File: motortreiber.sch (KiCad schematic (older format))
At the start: 40 parts, among them P15 STP_Y, P16 STP_E0, P17 STP_X, P18 STP_E1, P19 STP_Z, U3 A4988-BO, U4 A4988-BO, U5 A4988-BO, U6 A4988-BO, U7 A4988-BO

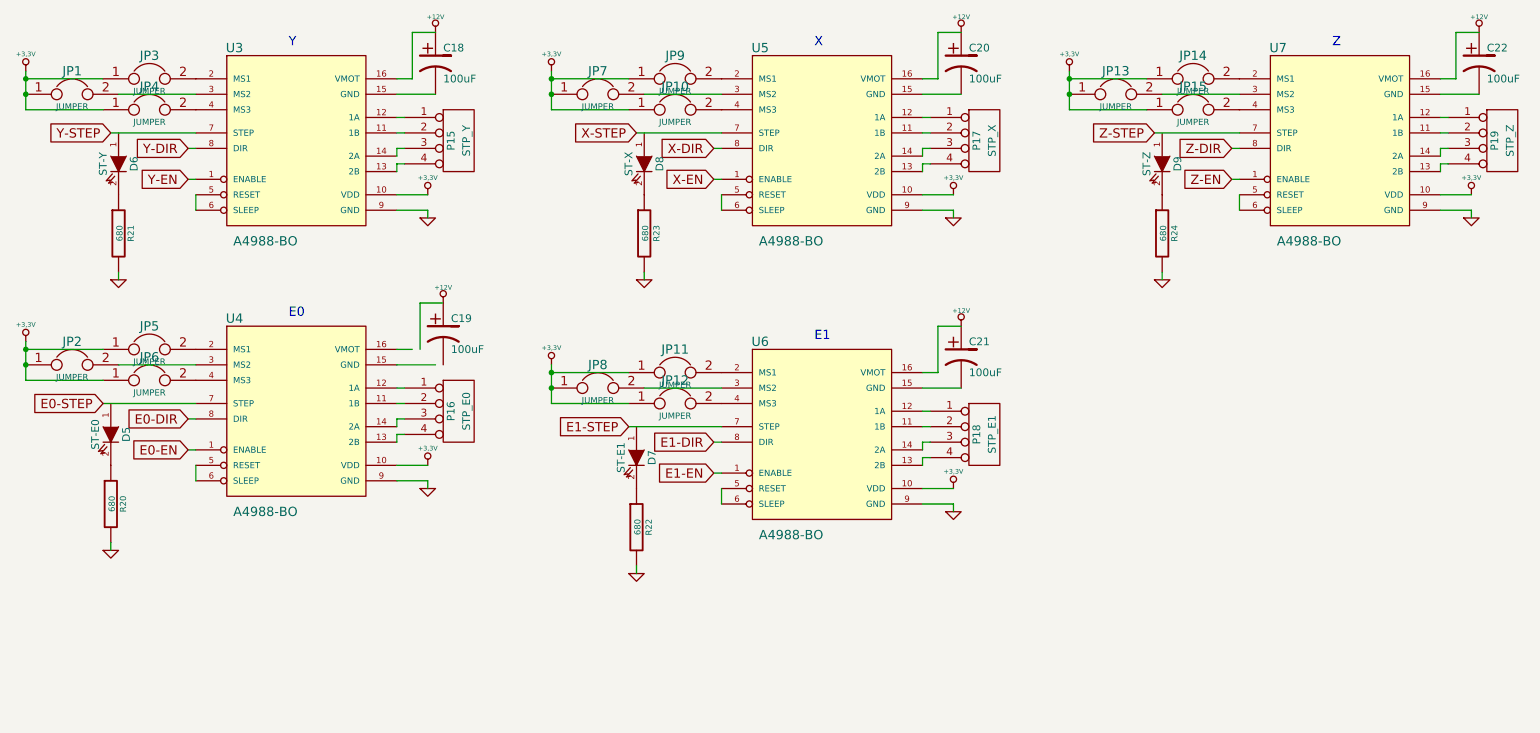
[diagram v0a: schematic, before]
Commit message: * Changed connectors to PSK type - this prevents plugging the steppers in the wrong way * Changed stepping increment jumpers to DIP-switches - easier setting
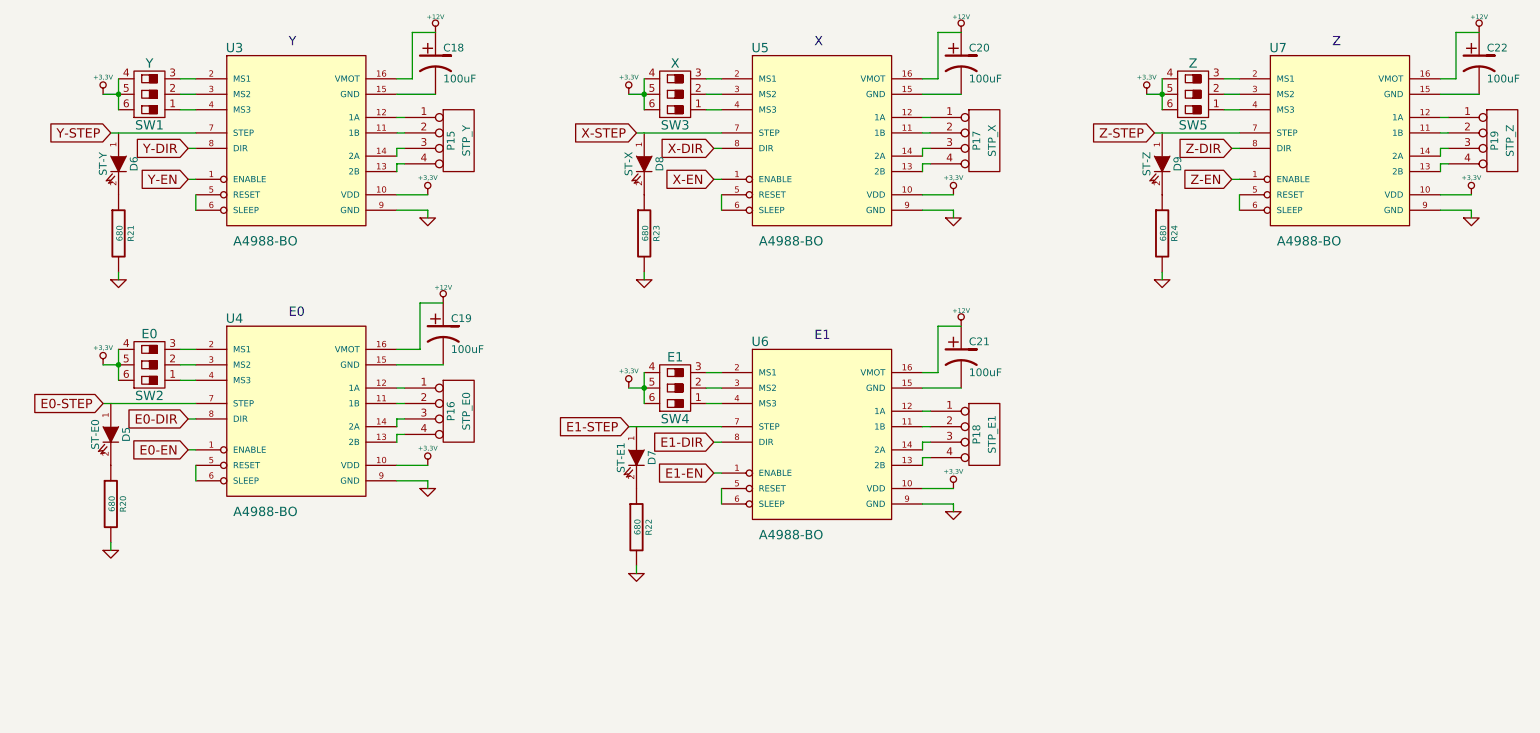
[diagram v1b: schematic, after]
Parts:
- removed JP1, JP10, JP11, JP12, JP13, JP14, JP15, JP2, JP3, JP4, JP5, JP6, JP7, JP8, JP9: JUMPER, ~, symbol JUMPER
- added SW1: Y, symbol DIPS_03
- added SW2: E0, symbol DIPS_03
- added SW3: X, symbol DIPS_03
- added SW4: E1, symbol DIPS_03
- added SW5: Z, symbol DIPS_03
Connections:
- net +12V: now also U4.16 (VMOT)
- net +3.3V: now also SW1.4, SW1.5, SW1.6, SW2.4, SW2.5, SW2.6, SW3.4, SW3.5, SW3.6, SW4.4, SW4.5, SW4.6, SW5.4, SW5.5, SW5.6
- net at U3.2 (MS1): now also SW1.3
- net at U3.3 (MS2): now also SW1.2
- net at U3.4 (MS3): now also SW1.1
- net at U5.2 (MS1): now also SW3.3
- net at U5.3 (MS2): now also SW3.2
- net at U5.4 (MS3): now also SW3.1
- net at U7.2 (MS1): now also SW5.3
- net at U7.3 (MS2): now also SW5.2
- net at U7.4 (MS3): now also SW5.1
- net at U4.15 (GND): now also C19.2
- net at U4.2 (MS1): now also SW2.3
- net at U4.3 (MS2): now also SW2.2
- net at U4.4 (MS3): now also SW2.1
- net at U6.2 (MS1): now also SW4.3
- net at U6.3 (MS2): now also SW4.2
- net at U6.4 (MS3): now also SW4.1

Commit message: * Removed numerous errors, schematic now passes ERC test. * Arranged footprints on PCB to prepare for routing
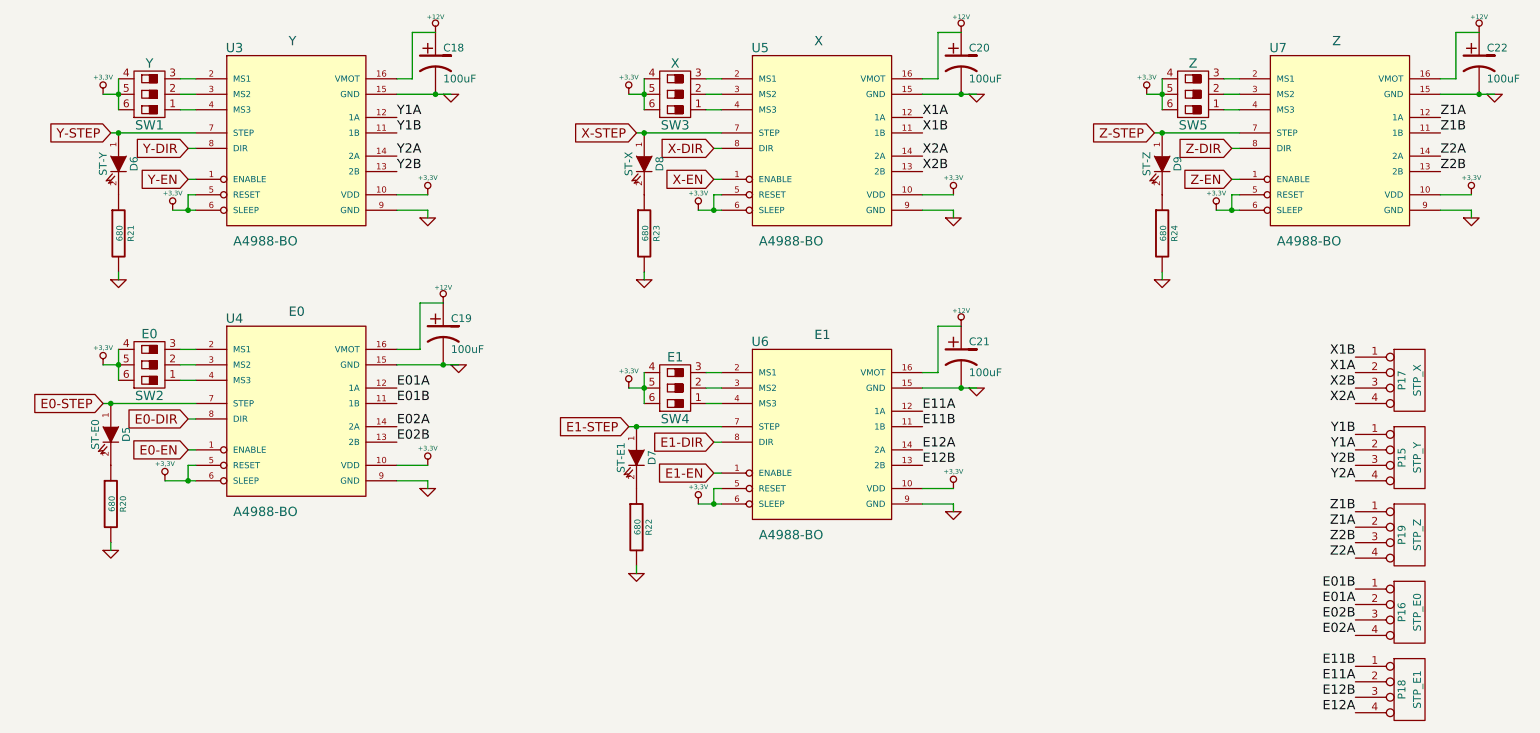
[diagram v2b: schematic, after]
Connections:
- net +3.3V: now also U3.5 (RESET), U3.6 (SLEEP), U4.5 (RESET), U4.6 (SLEEP), U5.5 (RESET), U5.6 (SLEEP), U6.5 (RESET), U6.6 (SLEEP), U7.5 (RESET), U7.6 (SLEEP)
- net E0-STEP: now also D5.1 (A)
- net E1-STEP: now also D7.1 (A)
- net GND: now also C18.2, C19.2, C20.2, C21.2, C22.2, U3.15 (GND), U4.15 (GND), U5.15 (GND), U6.15 (GND), U7.15 (GND)
- net X-STEP: now also D8.1 (A)
- net Y-STEP: now also D6.1 (A)
- net Z-STEP: now also D9.1 (A)
- net Y1A: now reaches P15.2 (P2)
- net Y1A: now also U3.12 (1A); no longer U3.11 (1B)
- net Y1B: now reaches P15.1 (P1)
- net Y1B: now also U3.11 (1B); no longer U3.12 (1A)
- net Y2A: now reaches P15.4 (P4)
- net Y2A: now also U3.14 (2A); no longer U3.13 (2B)
- net Y2B: now reaches P15.3 (P3)
- net Y2B: now also U3.13 (2B); no longer U3.14 (2A)
- net X1A: now reaches P17.2 (P2)
- net X1A: now also U5.12 (1A); no longer U5.11 (1B)
- net X1B: now reaches P17.1 (P1)
- net X1B: now also U5.11 (1B); no longer U5.12 (1A)
- net X2A: now reaches P17.4 (P4)
- net X2A: now also U5.14 (2A); no longer U5.13 (2B)
- net X2B: now reaches P17.3 (P3)
- net X2B: now also U5.13 (2B); no longer U5.14 (2A)
- net Z1A: now reaches P19.2 (P2)
- net Z1A: now also U7.12 (1A); no longer U7.11 (1B)
- net Z1B: now reaches P19.1 (P1)
- net Z1B: now also U7.11 (1B); no longer U7.12 (1A)
- net Z2A: now reaches P19.4 (P4)
- net Z2A: now also U7.14 (2A); no longer U7.13 (2B)
- net Z2B: now reaches P19.3 (P3)
- net Z2B: now also U7.13 (2B); no longer U7.14 (2A)
- net E01A: now reaches P16.2 (P2)
- net E01A: now also U4.12 (1A); no longer U4.11 (1B)
- net E01B: now reaches P16.1 (P1)
- net E01B: now also U4.11 (1B); no longer U4.12 (1A)
- net E02A: now reaches P16.4 (P4)
- net E02A: now also U4.14 (2A); no longer U4.13 (2B)
- net E02B: now reaches P16.3 (P3)
- net E02B: now also U4.13 (2B); no longer U4.14 (2A)
- net E11A: now reaches P18.2 (P2)
- net E11A: now also U6.12 (1A); no longer U6.11 (1B)
- net E11B: now reaches P18.1 (P1)
- net E11B: now also U6.11 (1B); no longer U6.12 (1A)
- net E12A: now reaches P18.4 (P4)
- net E12A: now also U6.14 (2A); no longer U6.13 (2B)
- net E12B: now reaches P18.3 (P3)
- net E12B: now also U6.13 (2B); no longer U6.14 (2A)
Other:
- moved on the sheet: P15, P16, P17, P18, P19

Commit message: * Schematic: Added decoupling cap for XMega * Schematic: Changed connector pin assignment for easier routing * Board: Changed arrangement of some components * Board: Routed all signal nets. To Do: Power nets.
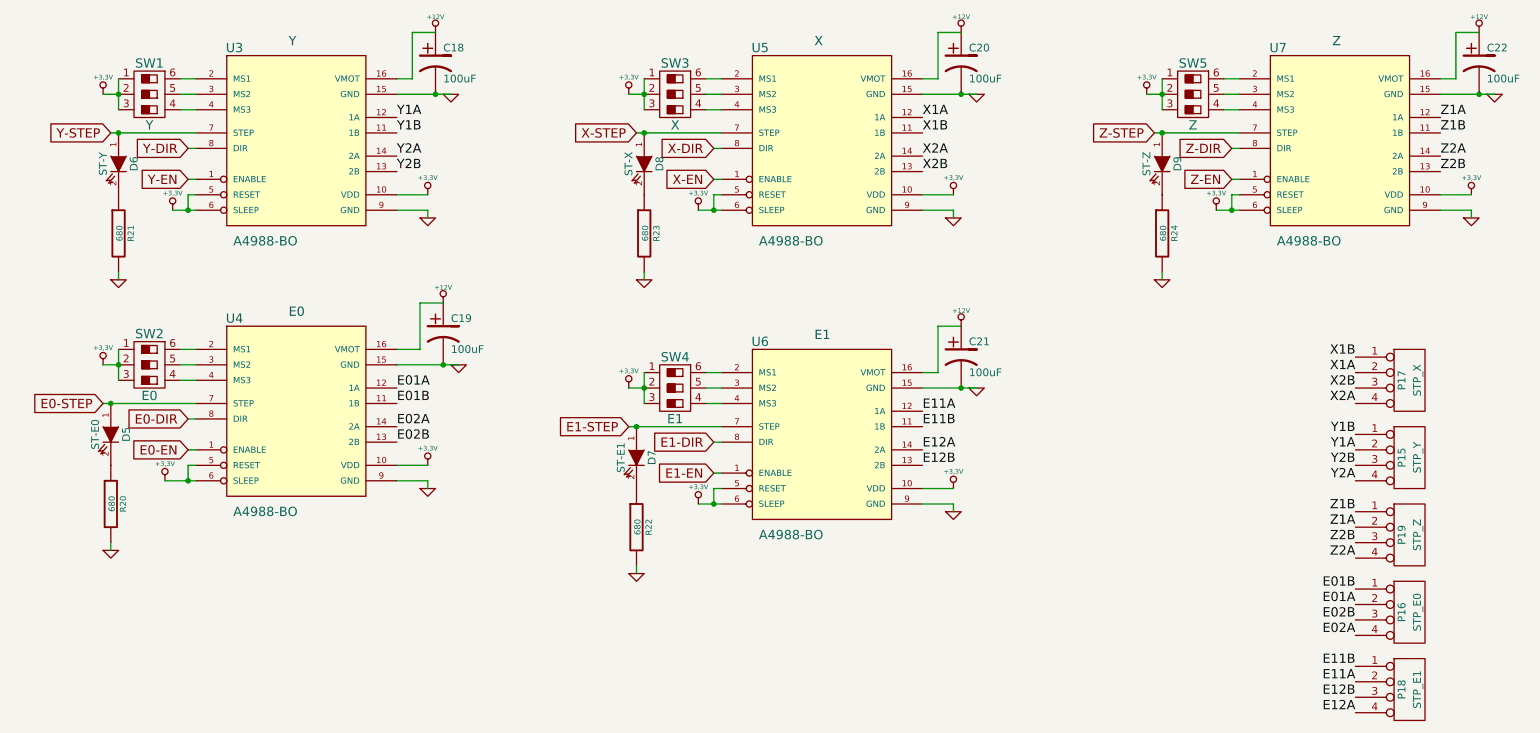
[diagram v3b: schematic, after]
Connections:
- net +3.3V: now also SW1.1, SW1.2, SW1.3, SW2.1, SW2.2, SW2.3, SW3.1, SW3.2, SW3.3, SW4.1, SW4.2, SW4.3, SW5.1, SW5.2, SW5.3; no longer SW1.4, SW1.5, SW1.6, SW2.4, SW2.5, SW2.6, SW3.4, SW3.5, SW3.6, SW4.4, SW4.5, SW4.6, SW5.4, SW5.5, SW5.6
- net at U3.2 (MS1): now also SW1.6; no longer SW1.3
- net at U3.3 (MS2): now also SW1.5; no longer SW1.2
- net at U3.4 (MS3): now also SW1.4; no longer SW1.1
- net at U5.2 (MS1): now also SW3.6; no longer SW3.3
- net at U5.3 (MS2): now also SW3.5; no longer SW3.2
- net at U5.4 (MS3): now also SW3.4; no longer SW3.1
- net at U7.2 (MS1): now also SW5.6; no longer SW5.3
- net at U7.3 (MS2): now also SW5.5; no longer SW5.2
- net at U7.4 (MS3): now also SW5.4; no longer SW5.1
- net at U4.2 (MS1): now also SW2.6; no longer SW2.3
- net at U4.3 (MS2): now also SW2.5; no longer SW2.2
- net at U4.4 (MS3): now also SW2.4; no longer SW2.1
- net at U6.2 (MS1): now also SW4.6; no longer SW4.3
- net at U6.3 (MS2): now also SW4.5; no longer SW4.2
- net at U6.4 (MS3): now also SW4.4; no longer SW4.1
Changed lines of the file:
@@
 F 3 "" H 5200 3050 60  0000 C CNN
 	1    5200 3050
-	0    -1   -1   0
+	0    1    1    0
 $EndComp
 $Comp
@@
 F 3 "" H 5200 1150 60  0000 C CNN
 	1    5200 1150
-	0    -1   -1   0
+	0    1    1    0
 $EndComp
 $Comp
@@
 F 3 "" H 8550 1150 60  0000 C CNN
 	1    8550 1150
-	0    -1   -1   0
+	0    1    1    0
 $EndComp
 $Comp
@@
 F 3 "" H 1800 1150 60  0000 C CNN
 	1    1800 1150
-	0    -1   -1   0
+	0    1    1    0
 $EndComp
 $Comp
@@
 F 3 "" H 1800 2900 60  0000 C CNN
 	1    1800 2900
-	0    -1   -1   0
+	0    1    1    0
 $EndComp
 $Comp
